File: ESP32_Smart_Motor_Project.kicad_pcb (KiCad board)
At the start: 2 copper layers, 163 x 131 mm, 14 parts, among them Q1 IRLZ34N

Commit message: minor changes
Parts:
- moved R5 50.6 mm to (179.3, 87.2), turned to 0 degrees
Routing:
- net Net-(L1-HV): track 70.8 -> 26.4 mm
- net /5V: track 376.8 -> 372.7 mm, vias 0 -> 2

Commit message: 19-apr-2026
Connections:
- D1 pad 1: /GPIO27 -> /3V3
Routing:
- net /GPIO27: track 133.1 -> 99.6 mm
- net /3V3: track 328.7 -> 349.5 mm, vias 2 -> 4
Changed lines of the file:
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@@
 			(crossoutdnponfab yes)
 			(subtractmaskfromsilk no)
-			(outputformat 1)
+			(outputformat 4)
 			(mirror no)
 			(drillshape 0)
@@
 			(layers "*.Cu" "*.Mask")
 			(remove_unused_layers no)
-			(net "Net-(L1-HV)")
+			(net "Net-(L1-HV2)")
 			(pinfunction "HV2_2")
 			(pintype "passive")
@@
 			(layers "*.Cu" "*.Mask")
 			(remove_unused_layers no)
-			(net "Net-(L1-HV4)")
+			(net "Net-(L1-HV3)")
 			(pinfunction "HV3_5")
 			(pintype "passive")
@@
 			(layers "*.Cu" "*.Mask")
 			(remove_unused_layers no)
-			(net "Net-(L1-LV2)")
+			(net "Net-(L1-HV4)")
 			(pinfunction "HV4_6")
 			(pintype "passive")
@@
 			(layers "*.Cu" "*.Mask")
 			(remove_unused_layers no)
-			(net "Net-(L1-HV)")
+			(net "Net-(L1-HV2)")
 			(pinfunction "SIG_3")
 			(pintype "passive")
@@
 			(layers "*.Cu" "*.Mask")
 			(remove_unused_layers no)
-			(net "Net-(L1-LV2)")
+			(net "Net-(L1-HV4)")
 			(pinfunction "RX_2")
 			(pintype "passive")
@@
 			(layers "*.Cu" "*.Mask")
 			(remove_unused_layers no)
-			(net "Net-(L1-HV4)")
+			(net "Net-(L1-HV3)")
 			(pinfunction "TX_3")
 			(pintype "passive")
@@
 			(layers "*.Cu" "*.Mask")
 			(remove_unused_layers no)
-			(net "/GPIO27")
+			(net "/3V3")
 			(pinfunction "LED_1")
 			(pintype "passive")
@@
 	)
 	(segment
+		(start 71.345 148.98)
+		(end 74.02 148.98)
+		(width 1)
+		(layer "F.Cu")
+		(net "/3V3")
+	)
+	(segment
 		(start 106 54)
 		(end 107.385 55.385)
@@
 	)
 	(segment
+		(start 74.02 148.98)
+		(end 80.5 142.5)
+		(width 1)
+		(layer "F.Cu")
+		(net "/3V3")
+	)
+	(segment
 		(start 137.805 140.98)
 		(end 129.655 140.98)
@@
 	)
 	(segment
-		(start 71.5 139)
+		(start 74 136.5)
 		(end 77 133.5)
 		(width 1)
@@
 	)
 	(segment
+		(start 71.5 139)
+		(end 74 136.5)
+		(width 1)
+		(layer "F.Cu")
+		(net "/3V3")
+	)
+	(segment
 		(start 154 136.5)
 		(end 147.5 143)
@@
 	)
 	(via
+		(at 80.5 142.5)
+		(size 2)
+		(drill 1)
+		(layers "F.Cu" "B.Cu")
+		(net "/3V3")
+	)
+	(via
 		(at 154 123.5)
 		(size 2)
@@
 		(net "/3V3")
 	)
+	(via
+		(at 74 136.5)
+		(size 2)
+		(drill 1)
+		(layers "F.Cu" "B.Cu")
+		(net "/3V3")
+	)
+	(segment
+		(start 80 142.5)
+		(end 74 136.5)
+		(width 1)
+		(layer "B.Cu")
+		(net "/3V3")
+	)
 	(segment
 		(start 154 123.5)
@@
 	)
 	(segment
+		(start 80.5 142.5)
+		(end 80 142.5)
+		(width 1)
+		(layer "B.Cu")
+		(net "/3V3")
+	)
+	(segment
 		(start 99.476878 99.562664)
 		(end 99.335456 99.421242)
@@
 	)
 	(segment
-		(start 161 97.802944)
-		(end 166.802944 92)
-		(width 1)
-		(layer "F.Cu")
-		(net "Net-(L1-HV)")
-	)
-	(segment
-		(start 176.5 92)
-		(end 177.5 91)
-		(width 1)
-		(layer "F.Cu")
-		(net "Net-(L1-HV)")
-	)
-	(segment
-		(start 161 101.54)
-		(end 161 97.802944)
-		(width 1)
-		(layer "F.Cu")
-		(net "Net-(L1-HV)")
-	)
-	(segment
-		(start 166.802944 92)
-		(end 176.5 92)
-		(width 1)
-		(layer "F.Cu")
-		(net "Net-(L1-HV)")
-	)
-	(segment
-		(start 160.04 102.5)
-		(end 161 101.54)
-		(width 1)
-		(layer "F.Cu")
-		(net "Net-(L1-HV)")
-	)
-	(segment
-		(start 177.5 91)
-		(end 177.5 89)
-		(width 1)
-		(layer "F.Cu")
-		(net "Net-(L1-HV)")
-	)
-	(segment
-		(start 134.505 117.995)
-		(end 134.505 119.98)
-		(width 1)
-		(layer "F.Cu")
-		(net "Net-(L1-HV4)")
-	)
-	(segment
-		(start 167.66 102.5)
-		(end 161.16 109)
-		(width 1)
-		(layer "F.Cu")
-		(net "Net-(L1-HV4)")
-	)
-	(segment
-		(start 143.5 109)
-		(end 134.505 117.995)
-		(width 1)
-		(layer "F.Cu")
-		(net "Net-(L1-HV4)")
-	)
-	(segment
-		(start 161.16 109)
-		(end 143.5 109)
-		(width 1)
-		(layer "F.Cu")
-		(net "Net-(L1-HV4)")
-	)
-	(segment
 		(start 170.2 102.5)
 		(end 162.2 110.5)
 		(width 1)
 		(layer "F.Cu")
-		(net "Net-(L1-LV2)")
+		(net "Net-(L1-HV4)")
 	)
 	(segment
@@
 		(width 1)
 		(layer "F.Cu")
-		(net "Net-(L1-LV2)")
+		(net "Net-(L1-HV4)")
 	)
 	(segment
@@
 		(width 1)
 		(layer "F.Cu")
-		(net "Net-(L1-LV2)")
+		(net "Net-(L1-HV4)")
 	)
 	(segment
@@
 		(width 1)
 		(layer "F.Cu")
-		(net "Net-(L1-LV2)")
-	)
-	(segment
-		(start 84.5 139.5)
-		(end 84.5 128.5)
-		(width 1)
-		(layer "F.Cu")
-		(net "/GPIO27")
-	)
-	(segment
-		(start 87.5 126.5)
-		(end 87.515 126.485)
-		(width 1)
-		(layer "F.Cu")
-		(net "/GPIO27")
-	)
-	(segment
-		(start 87.515 126.485)
-		(end 89.015 126.485)
-		(width 1)
-		(layer "F.Cu")
-		(net "/GPIO27")
+		(net "Net-(L1-HV4)")
 	)
 	(segment
@@
 	)
 	(segment
-		(start 86.5 126.5)
-		(end 87.5 126.5)
-		(width 1)
-		(layer "F.Cu")
-		(net "/GPIO27")
-	)
-	(segment
 		(start 155.75 115.5)
 		(end 146 115.5)
@@
 	)
 	(segment
-		(start 75.02 148.98)
-		(end 84.5 139.5)
-		(width 1)
-		(layer "F.Cu")
-		(net "/GPIO27")
-	)
-	(segment
 		(start 101.5 111.5)
 		(end 101.5 121)
@@
 		(net "/GPIO27")
 	)
-	(segment
-		(start 84.5 128.5)
-		(end 86.5 126.5)
-		(width 1)
-		(layer "F.Cu")
-		(net "/GPIO27")
-	)
-	(segment
-		(start 71.345 148.98)
-		(end 75.02 148.98)
-		(width 1)
-		(layer "F.Cu")
-		(net "/GPIO27")
-	)
 	(via
 		(at 146 115.5)
@@
 		(net "/GPIO25")
 	)
+	(segment
+		(start 161 97.802944)
+		(end 166.802944 92)
+		(width 1)
+		(layer "F.Cu")
+		(net "Net-(L1-HV2)")
+	)
+	(segment
+		(start 176.5 92)
+		(end 177.5 91)
+		(width 1)
+		(layer "F.Cu")
+		(net "Net-(L1-HV2)")
+	)
+	(segment
+		(start 161 101.54)
+		(end 161 97.802944)
+		(width 1)
+		(layer "F.Cu")
+		(net "Net-(L1-HV2)")
+	)
+	(segment
+		(start 166.802944 92)
+		(end 176.5 92)
+		(width 1)
+		(layer "F.Cu")
+		(net "Net-(L1-HV2)")
+	)
+	(segment
+		(start 160.04 102.5)
+		(end 161 101.54)
+		(width 1)
+		(layer "F.Cu")
+		(net "Net-(L1-HV2)")
+	)
+	(segment
+		(start 177.5 91)
+		(end 177.5 89)
+		(width 1)
+		(layer "F.Cu")
+		(net "Net-(L1-HV2)")
+	)
+	(segment
+		(start 134.505 117.995)
+		(end 134.505 119.98)
+		(width 1)
+		(layer "F.Cu")
+		(net "Net-(L1-HV3)")
+	)
+	(segment
+		(start 167.66 102.5)
+		(end 161.16 109)
+		(width 1)
+		(layer "F.Cu")
+		(net "Net-(L1-HV3)")
+	)
+	(segment
+		(start 143.5 109)
+		(end 134.505 117.995)
+		(width 1)
+		(layer "F.Cu")
+		(net "Net-(L1-HV3)")
+	)
+	(segment
+		(start 161.16 109)
+		(end 143.5 109)
+		(width 1)
+		(layer "F.Cu")
+		(net "Net-(L1-HV3)")
+	)
 	(zone

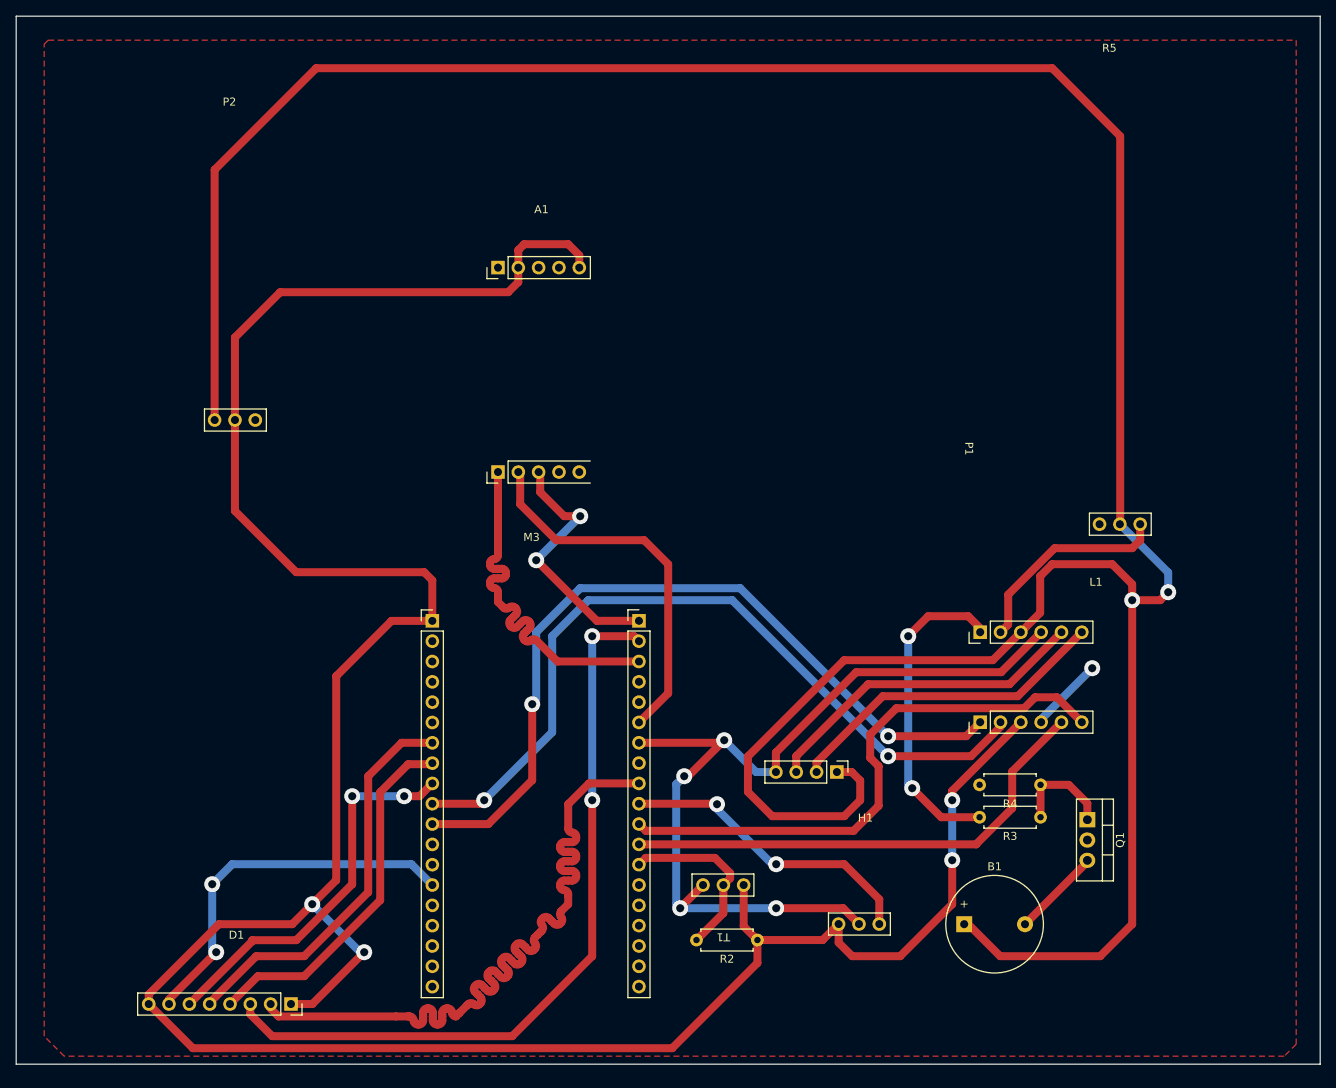
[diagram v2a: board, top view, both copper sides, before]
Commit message: make changes to board size
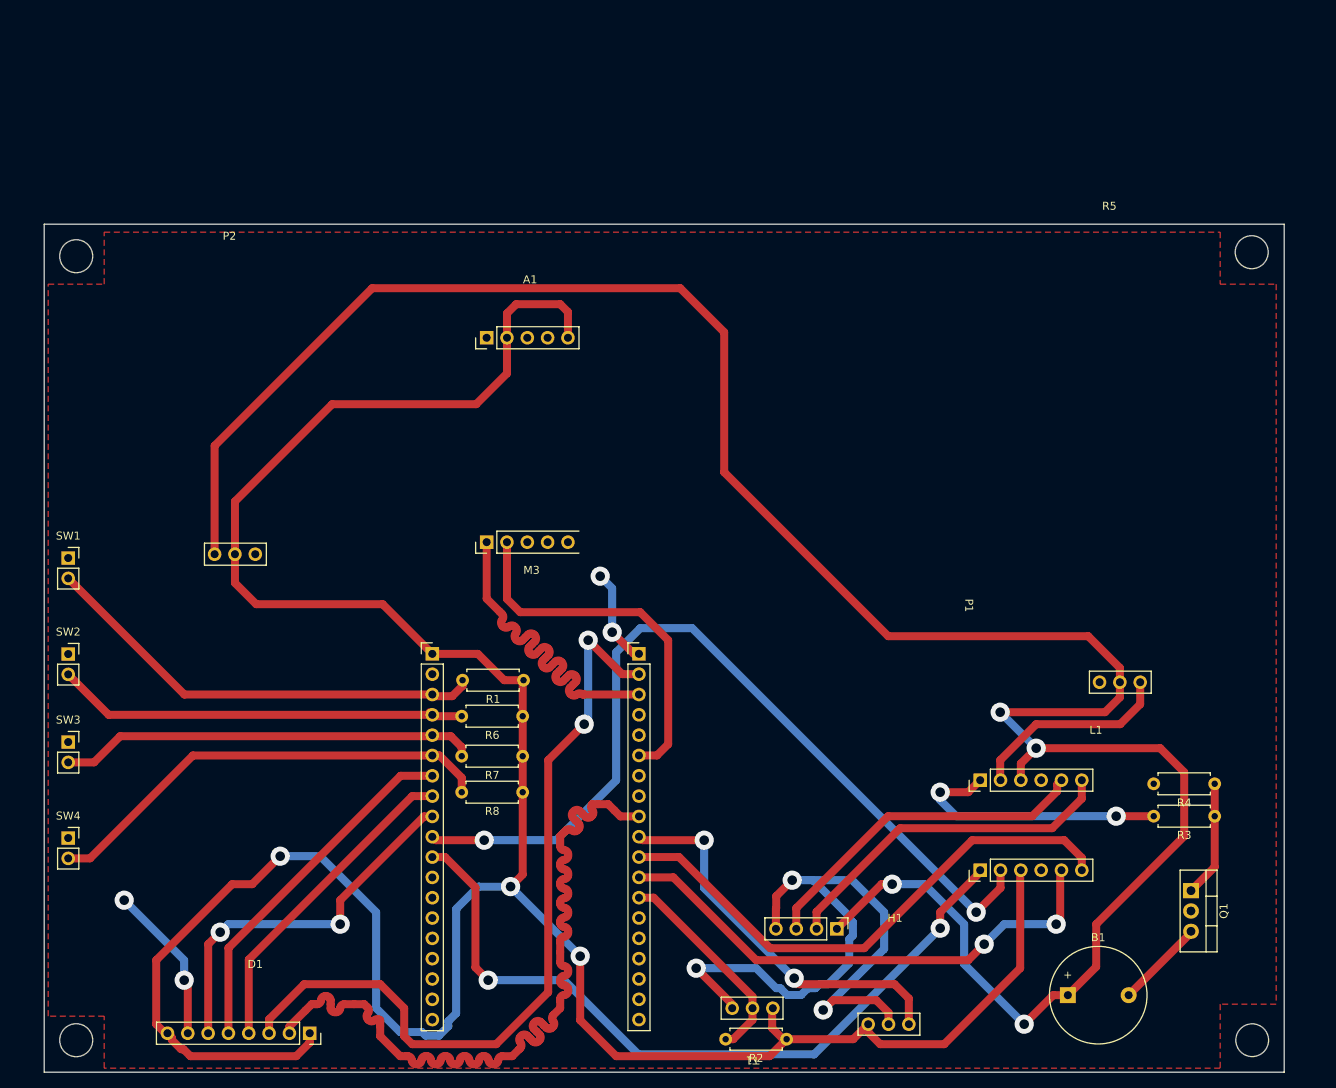
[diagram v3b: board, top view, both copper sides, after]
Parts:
- added R1: 10K, Resistor_THT:R_Axial_DIN0207_L6.3mm_D2.5mm_P7.62mm_Horizontal, F.Cu at (100.4, 108.5)
- added R6: 10K, Resistor_THT:R_Axial_DIN0207_L6.3mm_D2.5mm_P7.62mm_Horizontal, F.Cu at (100.3, 113.0)
- added R7: 10K, Resistor_THT:R_Axial_DIN0207_L6.3mm_D2.5mm_P7.62mm_Horizontal, F.Cu at (100.3, 118.0)
- added R8: 10K, Resistor_THT:R_Axial_DIN0207_L6.3mm_D2.5mm_P7.62mm_Horizontal, F.Cu at (100.3, 122.5)
- added SW1: SW_Push, Connector_PinSocket_2.54mm:PinSocket_1x02_P2.54mm_Vertical, F.Cu at (43.5, 93.2)
- added SW2: SW_Push, Connector_PinSocket_2.54mm:PinSocket_1x02_P2.54mm_Vertical, F.Cu at (43.5, 105.2)
- added SW3: SW_Push, Connector_PinSocket_2.54mm:PinSocket_1x02_P2.54mm_Vertical, F.Cu at (43.5, 116.2)
- added SW4: SW_Push, Connector_PinSocket_2.54mm:PinSocket_1x02_P2.54mm_Vertical, F.Cu at (43.5, 128.2)
- moved R3 21.8 mm to (186.8, 125.5)
- moved R4 21.8 mm to (186.8, 121.5)
- moved R5 19.8 mm to (179.3, 107.0)
- moved P1 19.6 mm to (136.1, 138.7)
- moved L1 18.5 mm to (172.0, 119.2)
- moved P2 16.8 mm to (68.7, 91.0)
- moved T1 15.8 mm to (129.0, 155.0)
- moved B1 15.7 mm to (168.5, 147.9)
- moved Q1 15.7 mm to (183.8, 134.8)
- moved H1 13.1 mm to (150.3, 149.7)
- moved R2 12.9 mm to (133.3, 153.4)
- moved A1 8.88 mm to (107.7, 63.9)
- moved D1 4.34 mm to (66.9, 144.5)
- moved M3 4.12 mm to (100.4, 110.8)
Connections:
- M3 pad 22: unconnected-(M3-GPIO36-Pad22) -> /GPIO36
- M3 pad 23: unconnected-(M3-GPIO39-Pad23) -> /GPIO39
- M3 pad 24: unconnected-(M3-GPIO34-Pad24) -> /GPIO34
- M3 pad 25: unconnected-(M3-GPIO35-Pad25) -> /GPIO35
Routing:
- net /5V: track 372.7 -> 291.9 mm, vias 2 -> 4
- net /GND: track 201.3 -> 122.5 mm, vias 9 -> 7
- net /GPIO35: track 0.00 -> 57.5 mm
- net /GPIO36: track 0.00 -> 56.6 mm
- net /GPIO34: track 0.00 -> 52.4 mm
- net /GPIO39: track 0.00 -> 51.8 mm
- net /GPIO5: track 38.4 -> 49.6 mm
- net /GPIO26: track 98.8 -> 109.7 mm
- net /HV1: track 40.3 -> 34.1 mm
- net /GPIO18: track 96.7 -> 102.0 mm
- net /GPIO23: track 95.4 -> 100.5 mm
- net /GPIO33: track 45.7 -> 40.6 mm
- net /GPIO32: track 49.9 -> 45.1 mm
- net /GPIO4: track 22.7 -> 26.6 mm
- net /GPIO27: track 99.6 -> 95.9 mm
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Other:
- board size 163 x 131 mm -> 155 x 106 mm

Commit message: 07-May-26
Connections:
- Q1 pad 2: /GND -> Net-(B1-GND)
- Q1 pad 3: Net-(B1-GND) -> /GND
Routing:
- net /GND: track 122.5 -> 102.8 mm, vias 7 -> 5
- net Net-(B1-GND): track 11.2 -> 15.9 mm
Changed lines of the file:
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@@
 	)
 	(paper "A4")
+	(title_block
+		(date "2026-05-07")
+		(rev "1")
+		(company "HARSHIL SUTHAR")
+	)
 	(layers
 		(0 "F.Cu" signal)
@@
 		(filling no)
 		(pcbplotparams
-			(layerselection 0x00000000_00000000_55555555_57555551)
+			(layerselection 0x00000000_00000000_55555555_57555555)
 			(plot_on_all_layers_selection 0x00000000_00000000_00000000_00000000)
 			(disableapertmacros no)
@@
 			(crossoutdnponfab yes)
 			(subtractmaskfromsilk no)
-			(outputformat 3)
+			(outputformat 4)
 			(mirror no)
 			(drillshape 0)
@@
 			(layers "*.Cu" "*.Mask")
 			(remove_unused_layers no)
-			(net "/GND")
+			(net "Net-(B1-GND)")
 			(pinfunction "D_2")
 			(pintype "passive")
@@
 			(layers "*.Cu" "*.Mask")
 			(remove_unused_layers no)
-			(net "Net-(B1-GND)")
+			(net "/GND")
 			(pinfunction "S_3")
 			(pintype "passive")
@@
 	)
 	(segment
+		(start 183.85 139.89)
+		(end 183.85 140.075)
+		(width 1)
+		(layer "F.Cu")
+		(net "/GND")
+	)
+	(segment
 		(start 134 133.5)
 		(end 132 135.5)
@@
 	)
 	(segment
-		(start 58.45 146.45)
-		(end 58 146)
-		(width 1)
-		(layer "F.Cu")
-		(net "/GND")
-	)
-	(segment
 		(start 114.205 105.205)
 		(end 111.5 102.5)
@@
 	)
 	(segment
-		(start 58.45 152.63)
-		(end 58.45 146.45)
-		(width 1)
-		(layer "F.Cu")
-		(net "/GND")
-	)
-	(segment
 		(start 132 135.5)
 		(end 132 137)
@@
 	)
 	(via
-		(at 50.5 136)
-		(size 2.4)
-		(drill 1.2)
-		(layers "F.Cu" "B.Cu")
-		(net "/GND")
-	)
-	(via
 		(at 137.873093 149.722743)
 		(size 2.4)
@@
 		(net "/GND")
 	)
-	(via
-		(at 58 146)
-		(size 2.4)
-		(drill 1.2)
-		(layers "F.Cu" "B.Cu")
-		(net "/GND")
-	)
 	(segment
 		(start 141.135 140.858427)
@@
 	)
 	(segment
-		(start 58 143.5)
-		(end 50.5 136)
-		(width 1)
-		(layer "B.Cu")
-		(net "/GND")
-	)
-	(segment
 		(start 129.5 144.5)
 		(end 132 147)
@@
 	)
 	(segment
-		(start 58 146)
-		(end 58 143.5)
-		(width 1)
-		(layer "B.Cu")
-		(net "/GND")
-	)
-	(segment
 		(start 145.5 142.095836)
 		(end 145.5 137.5)
@@
 	)
 	(segment
-		(start 183.85 139.89)
-		(end 183.85 140.075)
+		(start 176.055 147.87)
+		(end 178 145.925)
+		(width 1)
+		(layer "F.Cu")
+		(net "Net-(B1-GND)")
+	)
+	(segment
+		(start 178 139.5)
+		(end 180.15 137.35)
+		(width 1)
+		(layer "F.Cu")
+		(net "Net-(B1-GND)")
+	)
+	(segment
+		(start 178 145.925)
+		(end 178 139.5)
 		(width 1)
 		(layer "F.Cu")
@@
 	)
 	(segment
-		(start 183.85 140.075)
-		(end 176.055 147.87)
+		(start 180.15 137.35)
+		(end 183.85 137.35)
 		(width 1)
 		(layer "F.Cu")
